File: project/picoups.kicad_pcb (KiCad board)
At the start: 4 copper layers, 65 x 30 mm, 46 parts, among them J1 Conn_02x20_Odd_Even, J2 BATT, J3 VIN, J4 5V, Q1 Q_PMOS_GSD, U1 LT3652EMSE, U2 INA3221, U3 TPS61235P

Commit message: Ready for final check
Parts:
- added REF**: KiCad-Logo2_5mm_SilkScreen, Symbol:KiCad-Logo2_5mm_SilkScreen, F.Cu at (124.0, 107.0)
- added REF**: Logo_PicoUPS_Mixed, PicoUPS:Logo_PicoUPS_Mixed, F.Cu at (103.0, 107.0)
- added REF**: OSHW-Logo2_7.3x6mm_SilkScreen, Symbol:OSHW-Logo2_7.3x6mm_SilkScreen, F.Cu at (131.0, 107.0)
- moved TP3 0.50 mm to (94.0, 103.0)
- moved TP4 0.50 mm to (94.0, 107.0)
- moved TP5 0.50 mm to (94.0, 111.0)
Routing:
- net GND: track 20.7 -> 18.6 mm, vias 34 -> 33
- net Net-(U2-SDA): track 25.9 -> 26.9 mm
- net Net-(U2-SCL): track 26.7 -> 27.5 mm
- added copper zone on F.Cu, net GND
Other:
- board text added: "5V - +"
- board text added: "BAT - +"
- board text added: "JLCJLCJLCJLC"
- board text added: "VIN - +"
- board text added: "rev0.2 12-06-2023"

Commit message: Final version of this revision
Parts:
- C1, C4: footprint Capacitor_SMD:C_1206_3216Metric -> Capacitor_SMD:C_0805_2012Metric
- R7, R8, R9: value 0.005 -> 0.05
- moved REF** 2.25 mm to (105.2, 107.0)
- moved C4 0.55 mm to (134.3, 100.5)
- moved C1 0.50 mm to (137.5, 103.0)
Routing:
- net VBAT: track 2.68 -> 19.8 mm
- net /SENSE: track 0.00 -> 7.30 mm, vias 0 -> 2
- net /BOOST: track 0.00 -> 5.67 mm
- net /VFB: track 0.00 -> 2.11 mm
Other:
- board text added: "GND"
- board text added: "SCL"
- board text added: "SDA"
- board text added: "VINREG"
- board text added: "rev0.2.1 13-06-2023"
- board text removed: "rev0.2 12-06-2023"

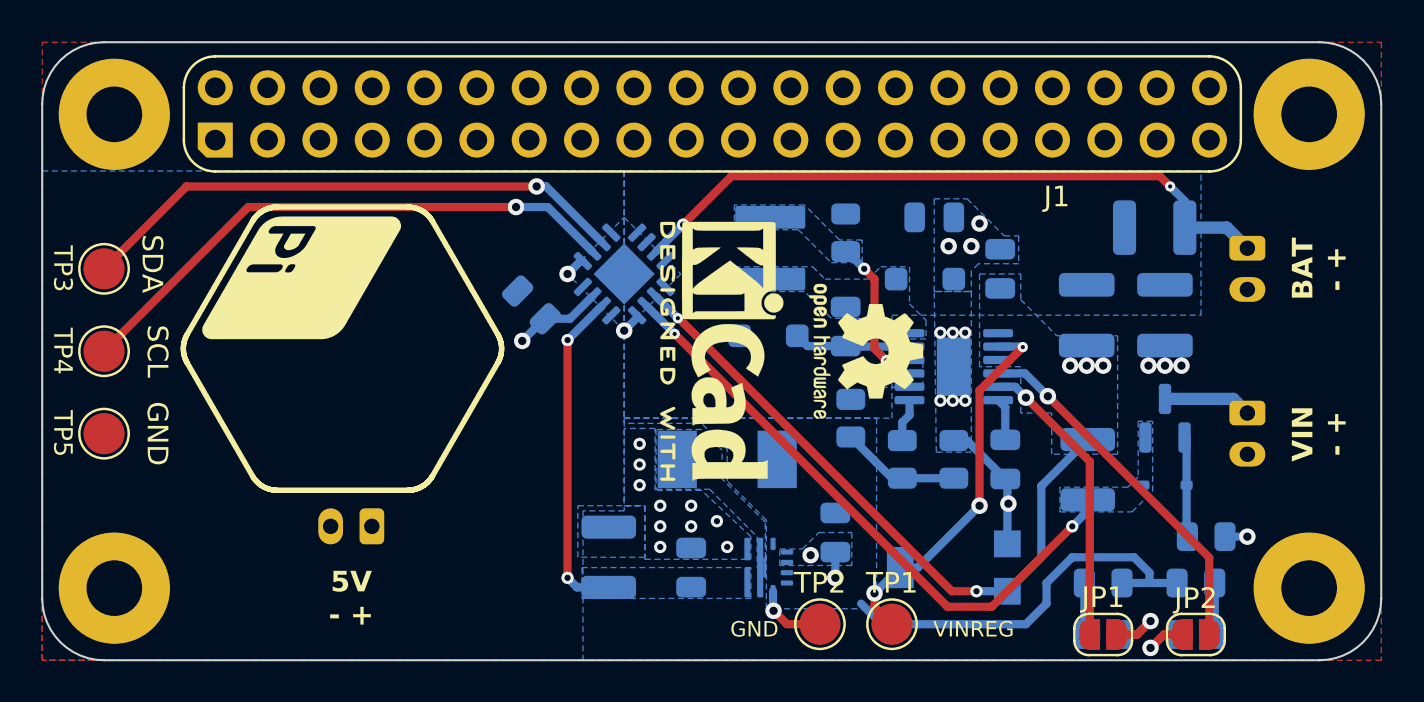
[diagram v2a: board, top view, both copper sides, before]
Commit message: Added footprints
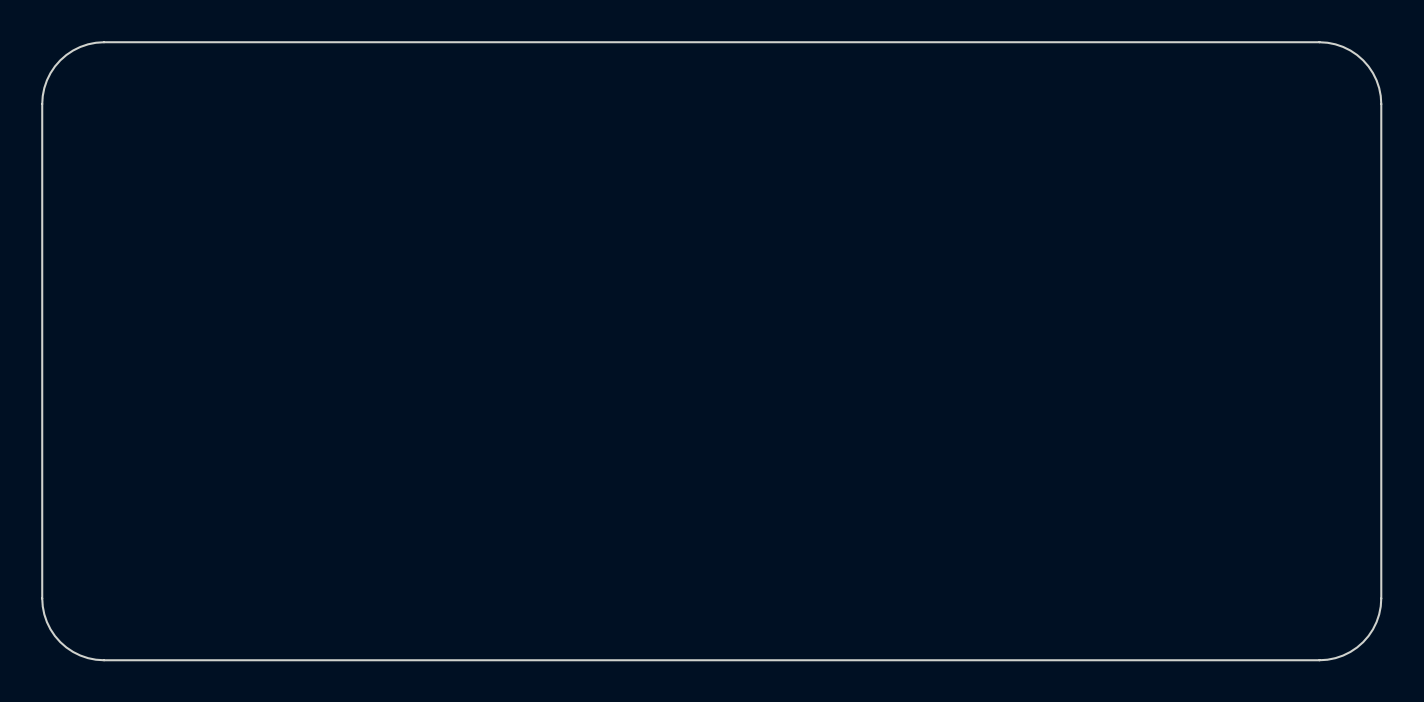
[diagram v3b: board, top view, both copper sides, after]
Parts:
- removed C1, C4, C8: 10uF, Capacitor_SMD:C_0805_2012Metric
- removed C10, C7: 22uF, Capacitor_SMD:C_0805_2012Metric
- removed C2, C3: 1uF, Capacitor_SMD:C_0805_2012Metric
- removed C5, C6: 47uF, Capacitor_SMD:C_1210_3225Metric
- removed D1, D2: 30V@3A, Diode_SMD:D_SOD-123F
- removed D3: CHRG, LED_SMD:LED_0805_2012Metric
- removed D4: FAULT, LED_SMD:LED_0805_2012Metric
- removed D5: 11V@300mW, Diode_SMD:D_SOD-323
- removed J1: Conn_02x20_Odd_Even, PicoUPS:PinSocket_2x20_P2.54mm_Vertical
- removed J2: BATT, Connector_JST:JST_PH_S2B-PH-K_1x02_P2.00mm_Horizontal
- removed J3: VIN, Connector_JST:JST_PH_S2B-PH-K_1x02_P2.00mm_Horizontal
- removed J4: 5V, Connector_JST:JST_PH_S2B-PH-K_1x02_P2.00mm_Horizontal
- removed JP1: FAULT_EN, Jumper:SolderJumper-2_P1.3mm_Open_RoundedPad1.0x1.5mm
- removed JP2: CHRG_EN, Jumper:SolderJumper-2_P1.3mm_Open_RoundedPad1.0x1.5mm
- removed L1: 8uH, Inductor_SMD:L_Abracon_ASPI-4030S
- removed L2: 1uH, Inductor_SMD:L_Vishay_IHLP-2020
- removed Q1: Q_PMOS_GSD, Package_TO_SOT_SMD:SOT-23
- removed R1: 0.066, Resistor_SMD:R_0805_2012Metric
- removed R11: 20k, Resistor_SMD:R_0805_2012Metric
- removed R2: 80k, Resistor_SMD:R_0805_2012Metric
- removed R3: 330k, Resistor_SMD:R_0805_2012Metric
- removed R4: 185k, Resistor_SMD:R_0805_2012Metric
- removed R5, R6: 260, Resistor_SMD:R_0805_2012Metric
- removed R7, R8, R9: 0.05, Resistor_SMD:R_1210_3225Metric
- removed REF**: KiCad-Logo2_5mm_SilkScreen, Symbol:KiCad-Logo2_5mm_SilkScreen
- removed REF**: Logo_PicoUPS_Mixed, PicoUPS:Logo_PicoUPS_Mixed
- removed REF**: OSHW-Logo2_7.3x6mm_SilkScreen, Symbol:OSHW-Logo2_7.3x6mm_SilkScreen
- removed REF** (x4): MountingHole_2.7mm_M2.5_Pad, MountingHole:MountingHole_2.7mm_M2.5_Pad
- removed RV1: 10k, PicoUPS:Potentiometer_Bourns_3214G_Horizontal
- removed TP1: VIN_REG, TestPoint:TestPoint_Pad_D2.0mm
- removed TP2, TP5: GND, TestPoint:TestPoint_Pad_D2.0mm
- removed TP3: SDA, TestPoint:TestPoint_Pad_D2.0mm
- removed TP4: SCL, TestPoint:TestPoint_Pad_D2.0mm
- removed U1: LT3652EMSE, Package_SO:MSOP-12-1EP_3x4mm_P0.65mm_EP1.65x2.85mm
- removed U2: INA3221, Package_DFN_QFN:Texas_RGV_S-PVQFN-N16_EP2.1x2.1mm
- removed U3: TPS61235P, PicoUPS:TPS61235P
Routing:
- net VBAT-: track 32.4 -> 0.00 mm, vias 2 -> 0
- net VIN: track 32.0 -> 0.00 mm, vias 2 -> 0
- net RAW: track 29.9 -> 0.00 mm, vias 2 -> 0
- net Net-(U2-SCL): track 27.5 -> 0.00 mm, vias 1 -> 0
- net Net-(U2-SDA): track 26.9 -> 0.00 mm, vias 1 -> 0
- net VBAT: track 19.8 -> 0.00 mm
- net GND: track 18.6 -> 0.00 mm, vias 33 -> 0
- net VIN_REG: track 18.5 -> 0.00 mm, vias 3 -> 0
- net CHRG: track 17.7 -> 0.00 mm, vias 1 -> 0
- net 5V+: track 16.1 -> 0.00 mm, vias 2 -> 0
- net FAULT: track 14.4 -> 0.00 mm, vias 1 -> 0
- net /SENSE: track 7.30 -> 0.00 mm, vias 2 -> 0
- net Net-(R2-Pad2): track 5.83 -> 0.00 mm
- net /BOOST: track 5.67 -> 0.00 mm
- net Net-(D5-A): track 4.87 -> 0.00 mm
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- removed copper zone on B.Cu, net /SENSE
- removed copper zone on B.Cu, net /SW
- removed copper zone on B.Cu, net 5V
- removed copper zone on B.Cu, net 5V+
- removed copper zone on B.Cu, net GND
- removed copper zone on F.Cu, net GND
- removed copper zone on B.Cu, net Net-(U3-SW)
- removed copper zone on B.Cu, net RAW
- removed copper zone on B.Cu, net VBAT
- removed copper zone on B.Cu, net VIN
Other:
- board text removed: "5V - +"
- board text removed: "BAT - +"
- board text removed: "GND"
- board text removed: "JLCJLCJLCJLC"
- board text removed: "SCL"
- board text removed: "SDA"
- board text removed: "VIN - +"
- board text removed: "VINREG"
- board text removed: "rev0.2.1 13-06-2023"

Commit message: Basic layout
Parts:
- added C1: 10uF, Capacitor_SMD:C_0805_2012Metric, B.Cu at (155.0, 71.0)
- added C10: 1uF, Capacitor_SMD:C_0805_2012Metric, B.Cu at (163.6, 120.7)
- added C11: 22uF, Capacitor_SMD:C_0805_2012Metric, B.Cu at (166.9, 107.0)
- added C2: 10uF, Capacitor_SMD:C_0805_2012Metric, B.Cu at (155.0, 75.0)
- added C3: 47uF, Capacitor_SMD:C_1210_3225Metric, B.Cu at (169.0, 76.0)
- added C4: 47uF, Capacitor_SMD:C_1210_3225Metric, B.Cu at (174.0, 76.0)
- added C5: 1uF, Capacitor_SMD:C_0805_2012Metric, B.Cu at (159.0, 77.0)
- added C6: 1uF, Capacitor_SMD:C_0805_2012Metric, B.Cu at (163.0, 77.0)
- added C7: 10uF, Capacitor_SMD:C_0805_2012Metric, B.Cu at (173.4, 100.7)
- added C8: 22uF, Capacitor_SMD:C_0805_2012Metric, B.Cu at (173.4, 103.7)
- added C9: 1uF, Capacitor_SMD:C_0805_2012Metric, B.Cu at (163.6, 117.7)
- added D1: 30V@3A, Diode_SMD:D_SOD-123F, B.Cu at (179.6, 76.0)
- added D2: 30V@3A, Diode_SMD:D_SOD-123F, B.Cu at (182.6, 71.0)
- added D3: 11V@300mW, Diode_SMD:D_SOD-323, B.Cu at (192.7, 128.0)
- added D4: FAULT, LED_SMD:LED_0805_2012Metric, B.Cu at (178.8, 117.7)
- added D5: CHRG, LED_SMD:LED_0805_2012Metric, B.Cu at (178.8, 120.7)
- added D6: CHRG, LED_SMD:LED_0805_2012Metric, B.Cu at (178.8, 123.8)
- added D7: PWRGD, LED_SMD:LED_0805_2012Metric, B.Cu at (178.8, 126.8)
- added J1: VIN, Connector_JST:JST_PH_S2B-PH-K_1x02_P2.00mm_Horizontal, B.Cu at (148.6, 102.0)
- added J2: BATT, Connector_JST:JST_PH_S2B-PH-K_1x02_P2.00mm_Horizontal, B.Cu at (148.6, 110.0)
- added J3: USB_C_Receptacle, Connector_USB:USB_C_Receptacle_GCT_USB4105-xx-A_16P_TopMnt_Horizontal, B.Cu at (132.4, 118.3)
- added J4: Conn_02x20_Odd_Even, PicoUPS:PinSocket_2x20_P2.54mm_Vertical, F.Cu at (99.4, 94.2)
- added JP1: USER, Jumper:SolderJumper-2_P1.3mm_Open_RoundedPad1.0x1.5mm, B.Cu at (192.7, 124.7)
- added JP2: FAULT, Jumper:SolderJumper-2_P1.3mm_Open_RoundedPad1.0x1.5mm, B.Cu at (183.3, 117.9)
- added JP3: CHRG, Jumper:SolderJumper-2_P1.3mm_Open_RoundedPad1.0x1.5mm, B.Cu at (183.3, 121.5)
- added JP4: CHRG, Jumper:SolderJumper-2_P1.3mm_Open_RoundedPad1.0x1.5mm, B.Cu at (183.3, 125.0)
- added JP5: PWRGD, Jumper:SolderJumper-2_P1.3mm_Open_RoundedPad1.0x1.5mm, B.Cu at (183.3, 128.6)
- added L1: 7.6uH, Inductor_SMD:L_Bourns-SRN6028, B.Cu at (171.0, 69.0)
- added L2: 1uH, Inductor_SMD:L_Vishay_IHLP-2020, B.Cu at (181.3, 109.4)
- added Q1: Q_PMOS_GSD, Package_TO_SOT_SMD:SOT-23, B.Cu at (192.5, 120.7)
- added R1: 0.066, Resistor_SMD:R_0805_2012Metric, B.Cu at (155.0, 67.0)
- added R10: 0.05, Resistor_SMD:R_1210_3225Metric, B.Cu at (200.5, 93.2)
- added R11: 0.05, Resistor_SMD:R_1210_3225Metric, B.Cu at (200.5, 97.4)
- added R12: 20k, Resistor_SMD:R_0805_2012Metric, B.Cu at (201.1, 115.9)
- added R13: 5.1k, Resistor_SMD:R_0603_1608Metric, B.Cu at (196.9, 119.8)
- added R14: 5.1k, Resistor_SMD:R_0603_1608Metric, B.Cu at (196.9, 122.3)
- added R15: 1M, Resistor_SMD:R_0805_2012Metric, B.Cu at (201.1, 118.9)
- added R16: 260, Resistor_SMD:R_0805_2012Metric, B.Cu at (174.4, 117.6)
- added R17: 260, Resistor_SMD:R_0805_2012Metric, B.Cu at (174.4, 120.6)
- added R18: 260, Resistor_SMD:R_0805_2012Metric, B.Cu at (174.4, 123.5)
- added R19: 260, Resistor_SMD:R_0805_2012Metric, B.Cu at (174.4, 126.5)
- added R2: 80k, Resistor_SMD:R_0805_2012Metric, B.Cu at (157.0, 59.0)
- added R3: 185k, Resistor_SMD:R_0805_2012Metric, B.Cu at (154.0, 63.0)
- added R4: 330k, Resistor_SMD:R_0805_2012Metric, B.Cu at (158.0, 63.0)
- added R5: 1M, Resistor_SMD:R_0805_2012Metric, B.Cu at (174.9, 112.7)
- added R6: 720, Resistor_SMD:R_0805_2012Metric, B.Cu at (168.0, 117.6)
- added R7: 2k, Resistor_SMD:R_0805_2012Metric, B.Cu at (168.0, 120.6)
- added R8: 10k, Resistor_SMD:R_0805_2012Metric, B.Cu at (168.0, 123.5)
- added R9: 0.05, Resistor_SMD:R_1210_3225Metric, B.Cu at (182.0, 64.0)
- added REF**: MountingHole, PicoUPS:MountingHole, F.Cu at (94.5, 118.5)
- added REF**: MountingHole, PicoUPS:MountingHole, F.Cu at (152.5, 95.5)
- added REF**: MountingHole, PicoUPS:MountingHole, F.Cu at (94.5, 95.5)
- added REF**: MountingHole, PicoUPS:MountingHole, F.Cu at (152.5, 118.5)
- added RV1: 10k, PicoUPS:Potentiometer_Bourns_3313J-1_Vertical, B.Cu at (162.0, 67.0)
- added SW1: SW_5V, PicoUPS:SW_SPDT_PCM12, B.Cu at (121.5, 120.0)
- added SW2: SW_USER, PicoUPS:SW_Push, B.Cu at (142.0, 120.5)
- added TP1: VIN_REG, TestPoint:TestPoint_Pad_D2.0mm, B.Cu at (177.0, 68.0)
- added TP2: GND, TestPoint:TestPoint_Pad_D2.0mm, B.Cu at (178.0, 72.0)
- added U1: LT3652EMSE, Package_SO:MSOP-12-1EP_3x4mm_P0.65mm_EP1.65x2.85mm, B.Cu at (161.6, 72.3)
- added U2: TPS2116, Package_TO_SOT_SMD:SOT-583-8, B.Cu at (167.3, 112.3)
- added U3: TPS61235P, PicoUPS:TPS61235P, B.Cu at (174.5, 108.6)
- added U4: BQ24040, PicoUPS:WSON-10-1EP_2x2mm_P0.5mm, B.Cu at (163.7, 124.0)
- added U5: INA3221, Package_DFN_QFN:Texas_RGV_S-PVQFN-N16_EP2.1x2.1mm, B.Cu at (166.0, 102.3)
- added U6: M41T62, PicoUPS:LCC-8, B.Cu at (196.2, 116.5)

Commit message: First layout of PCB
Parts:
- JP1, JP2, JP3, JP4, JP5, TP1, TP2: moved to F.Cu
- moved R15 106.7 mm to (94.5, 114.5)
- moved JP1 98.8 mm to (94.5, 114.5)
- moved U6 87.6 mm to (108.6, 112.5)
- moved R10 82.6 mm to (120.0, 111.5), turned to 0 degrees
- moved R11 82.0 mm to (119.2, 108.0)
- moved R12 75.3 mm to (126.0, 111.5), turned to -90 degrees
- moved JP2 74.7 mm to (108.6, 120.5)
- moved JP3 71.2 mm to (112.1, 120.5)
- moved D4 70.3 mm to (108.6, 120.5), turned to 0 degrees
- moved D5 66.8 mm to (112.1, 120.5), turned to 0 degrees
- moved R16 65.9 mm to (108.6, 118.5)
- moved R9 64.7 mm to (132.8, 106.0), turned to 90 degrees
- moved Q1 64.1 mm to (129.0, 111.5)
- moved RV1 63.5 mm to (123.5, 117.5)
- moved D3 62.9 mm to (132.0, 111.5), turned to 90 degrees
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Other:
- outline, holes or cut-outs redrawn

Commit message: Semi-final arrangement
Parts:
- moved TP1 38.9 mm to (146.2, 105.2)
- moved TP2 35.5 mm to (146.2, 108.8)
- moved R16 29.0 mm to (137.5, 116.5), turned to 90 degrees
- moved D4 28.9 mm to (137.5, 120.0), turned to 90 degrees
- moved JP2 28.9 mm to (137.5, 120.0), turned to -90 degrees
- moved R17 27.9 mm to (139.9, 116.5), turned to 90 degrees
- moved D5 27.8 mm to (139.9, 120.0), turned to 90 degrees
- moved JP3 27.8 mm to (139.9, 120.0), turned to -90 degrees
- moved RV1 26.5 mm to (144.8, 101.8), turned to 0 degrees
- moved C9 25.5 mm to (118.2, 103.2), turned to 90 degrees
- moved R6 25.3 mm to (120.2, 101.5), turned to -90 degrees
- moved R7 23.4 mm to (122.2, 101.5), turned to -90 degrees
- moved C10 22.8 mm to (118.2, 106.8), turned to 90 degrees
- moved C5 22.4 mm to (125.5, 101.3), turned to -90 degrees
- moved L1 22.0 mm to (130.2, 102.8), turned to -90 degrees
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
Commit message: Final layout
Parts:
- U1: footprint Package_SO:MSOP-12-1EP_3x4mm_P0.65mm_EP1.65x2.85mm -> Package_SO:MSOP-12-1EP_3x4mm_P0.65mm_EP1.65x2.85mm_ThermalVias
- U5: footprint Package_DFN_QFN:Texas_RGV_S-PVQFN-N16_EP2.1x2.1mm -> Package_DFN_QFN:Texas_RGV_S-PVQFN-N16_EP2.1x2.1mm_ThermalVias
- moved R5 26.5 mm to (99.0, 100.8), turned to 180 degrees
- moved JP1 0.50 mm to (94.5, 114.0)
- moved C10 0.25 mm to (118.2, 106.5)
- moved C9 0.25 mm to (118.2, 103.0)
- moved R6 0.25 mm to (120.2, 101.2)
- moved R7 0.25 mm to (122.2, 101.2)
- moved R8 0.25 mm to (120.2, 108.2)
- moved U2 0.25 mm to (121.2, 113.0)
- moved U4 0.25 mm to (120.8, 104.8)
- moved C6 0.10 mm to (139.7, 109.0)
- moved D1 0.10 mm to (136.0, 100.4)
- moved R3 0.10 mm to (135.3, 109.0)
- turned R15 to 0 degrees
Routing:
- net Net-(J4-Pin_37): track 0.00 -> 74.4 mm
- net VBAT+: track 0.00 -> 74.0 mm, vias 0 -> 4
- net GND: track 0.00 -> 44.1 mm, vias 0 -> 32
- net USB_5V: track 0.00 -> 38.9 mm
- net Net-(SW1-C): track 0.00 -> 38.5 mm, vias 0 -> 2
- net /Status LEDs/USB_CHRG: track 0.00 -> 33.1 mm, vias 0 -> 1
- net /Status LEDs/USB_PWRGD: track 0.00 -> 32.5 mm, vias 0 -> 1
- net 5V+: track 0.00 -> 30.8 mm, vias 0 -> 3
- net VBAT-: track 0.00 -> 30.5 mm, vias 0 -> 2
- net VBAT_SOL-: track 0.00 -> 21.7 mm, vias 0 -> 2
- net SDA: track 0.00 -> 19.4 mm, vias 0 -> 1
- net VBAT_SOL+: track 0.00 -> 18.2 mm, vias 0 -> 2
- net /Solar Panel Supply/CHRG: track 0.00 -> 17.6 mm, vias 0 -> 1
- net /Solar Panel Supply/FAULT: track 0.00 -> 16.4 mm, vias 0 -> 1
- net 3v3: track 0.00 -> 14.4 mm, vias 0 -> 1
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- added copper zone on B.Cu, net /Solar Panel Supply/VIN
- added copper zone on B.Cu, net 5V
- added copper zone on B.Cu, net 5V+
- added copper zone on B.Cu, net GND
- added copper zone on F.Cu, net GND
- added copper zone on B.Cu, net USB_5V
- added copper zone on B.Cu, net VBAT+
- added copper zone on B.Cu, net VBAT_SOL+

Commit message: Labels final position
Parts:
- moved R12 0.40 mm to (139.0, 112.5)
- moved R8 0.25 mm to (120.2, 108.5)
